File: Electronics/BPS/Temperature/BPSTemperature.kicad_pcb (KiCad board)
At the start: 2 copper layers, 0 parts

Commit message: Created PCB of Temperture Board for BPS
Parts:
- added C1: 1uF, Capacitor_SMD:C_0805_2012Metric, F.Cu at (66.6, 83.7)
- added C10: 1uF, Capacitor_SMD:C_0805_2012Metric, F.Cu at (66.7, 113.6)
- added C11: 1uF, Capacitor_SMD:C_0805_2012Metric, B.Cu at (66.6, 83.7)
- added C12: 1uF, Capacitor_SMD:C_0805_2012Metric, B.Cu at (66.6, 87.0)
- added C13: 1uF, Capacitor_SMD:C_0805_2012Metric, B.Cu at (66.6, 90.3)
- added C14: 1uF, Capacitor_SMD:C_0805_2012Metric, B.Cu at (66.6, 93.8)
- added C15: 1uF, Capacitor_SMD:C_0805_2012Metric, B.Cu at (66.6, 97.0)
- added C16: 1uF, Capacitor_SMD:C_0805_2012Metric, B.Cu at (66.6, 100.3)
- added C17: 1uF, Capacitor_SMD:C_0805_2012Metric, B.Cu at (66.6, 103.6)
- added C18: 1uF, Capacitor_SMD:C_0805_2012Metric, B.Cu at (66.6, 106.9)
- added C19: 1uF, Capacitor_SMD:C_0805_2012Metric, B.Cu at (66.7, 110.3)
- added C2: 1uF, Capacitor_SMD:C_0805_2012Metric, F.Cu at (66.5, 87.0)
- added C20: 1uF, Capacitor_SMD:C_0805_2012Metric, B.Cu at (66.6, 113.6)
- added C21: 0.1uF, Capacitor_SMD:C_0805_2012Metric, F.Cu at (90.5, 91.2)
- added C22: 10uF, Capacitor_SMD:C_0805_2012Metric, F.Cu at (93.3, 99.9)
- added C23: 10uF, Capacitor_SMD:C_0805_2012Metric, F.Cu at (88.5, 105.3)
- added C24: 10uF, Capacitor_SMD:C_0805_2012Metric, F.Cu at (92.3, 103.3)
- added C25: 1uF, Capacitor_SMD:C_0805_2012Metric, F.Cu at (87.5, 88.0)
- added C26: 1uF, Capacitor_SMD:C_0805_2012Metric, F.Cu at (83.4, 88.0)
- added C3: 1uF, Capacitor_SMD:C_0805_2012Metric, F.Cu at (66.6, 90.4)
- added C4: 1uF, Capacitor_SMD:C_0805_2012Metric, F.Cu at (66.6, 93.7)
- added C5: 1uF, Capacitor_SMD:C_0805_2012Metric, F.Cu at (66.5, 97.0)
- added C6: 1uF, Capacitor_SMD:C_0805_2012Metric, F.Cu at (66.6, 100.3)
- added C7: 1uF, Capacitor_SMD:C_0805_2012Metric, F.Cu at (66.6, 103.6)
- added C8: 1uF, Capacitor_SMD:C_0805_2012Metric, F.Cu at (66.5, 106.9)
- added C9: 1uF, Capacitor_SMD:C_0805_2012Metric, F.Cu at (66.6, 110.3)
- added D1: LED, LED_SMD:LED_0805_2012Metric, F.Cu at (103.1, 126.0)
- added J1: Conn_02x10_Counter_Clockwise, Connector_Molex:Molex_Micro-Fit_3.0_43045-2012_2x10_P3.00mm_Vertical, F.Cu at (54.1, 113.3)
- added J2: Logic Analyzer, Connector_PinHeader_2.54mm:PinHeader_1x05_P2.54mm_Vertical, F.Cu at (100.4, 129.7)
- added J3: Conn_02x06_Counter_Clockwise, UTSVT_Connectors:Molex_MicroFit3.0_2x6xP3.00mm_PolarizingPeg_Vertical, F.Cu at (121.1, 102.4)
- added J4: Conn_02x06_Counter_Clockwise, UTSVT_Connectors:Molex_MicroFit3.0_2x6xP3.00mm_PolarizingPeg_Vertical, F.Cu at (121.1, 79.7)
- added MH1: MountingHole, MountingHole:MountingHole_3mm, F.Cu at (53.0, 70.0)
- added MH2: MountingHole, MountingHole:MountingHole_3mm, F.Cu at (53.0, 129.0)
- added MH3: MountingHole, MountingHole:MountingHole_3mm, F.Cu at (122.0, 129.0)
- added MH4: MountingHole, MountingHole:MountingHole_3mm, F.Cu at (122.0, 70.0)
- added R1: 1k, Resistor_SMD:R_0805_2012Metric, F.Cu at (62.6, 83.7)
- added R10: 1k, Resistor_SMD:R_0805_2012Metric, F.Cu at (62.6, 113.6)
- added R11: 1k, Resistor_SMD:R_0805_2012Metric, B.Cu at (62.6, 83.7)
- added R12: 1k, Resistor_SMD:R_0805_2012Metric, B.Cu at (62.6, 87.0)
- added R13: 1k, Resistor_SMD:R_0805_2012Metric, B.Cu at (62.6, 90.3)
- added R14: 1k, Resistor_SMD:R_0805_2012Metric, B.Cu at (62.6, 93.8)
- added R15: 1k, Resistor_SMD:R_0805_2012Metric, B.Cu at (62.6, 97.0)
- added R16: 1k, Resistor_SMD:R_0805_2012Metric, B.Cu at (62.6, 100.3)
- added R17: 1k, Resistor_SMD:R_0805_2012Metric, B.Cu at (62.6, 103.6)
- added R18: 1k, Resistor_SMD:R_0805_2012Metric, B.Cu at (62.6, 106.9)
- added R19: 1k, Resistor_SMD:R_0805_2012Metric, B.Cu at (62.6, 110.3)
- added R2: 1k, Resistor_SMD:R_0805_2012Metric, F.Cu at (62.6, 87.0)
- added R20: 1k, Resistor_SMD:R_0805_2012Metric, B.Cu at (62.6, 113.6)
- added R3: 1k, Resistor_SMD:R_0805_2012Metric, F.Cu at (62.6, 90.4)
- added R4: 1k, Resistor_SMD:R_0805_2012Metric, F.Cu at (62.6, 93.7)
- added R5: 1k, Resistor_SMD:R_0805_2012Metric, F.Cu at (62.6, 97.0)
- added R6: 1k, Resistor_SMD:R_0805_2012Metric, F.Cu at (62.6, 100.3)
- added R7: 1k, Resistor_SMD:R_0805_2012Metric, F.Cu at (62.6, 103.6)
- added R8: 1k, Resistor_SMD:R_0805_2012Metric, F.Cu at (62.6, 106.9)
- added R9: 1k, Resistor_SMD:R_0805_2012Metric, F.Cu at (62.6, 110.3)
- added SW1: SW_DIP_x06, Button_Switch_SMD:SW_DIP_SPSTx06_Slide_Omron_A6S-610x_W8.9mm_P2.54mm, F.Cu at (105.3, 98.5)
- added TP1: TestPoint, TestPoint:TestPoint_Keystone_5005-5009_Compact, F.Cu at (83.4, 121.7)
- added TP2: TestPoint, TestPoint:TestPoint_Keystone_5005-5009_Compact, F.Cu at (63.5, 121.4)
- added U1: LTC2983, Package_QFP:LQFP-48_7x7mm_P0.5mm, F.Cu at (83.4, 98.0)
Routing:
- net GND: track 0.00 -> 88.3 mm, vias 0 -> 15
- net Net-(C11-Pad1): track 0.00 -> 33.8 mm, vias 0 -> 1
- net Net-(C12-Pad1): track 0.00 -> 33.4 mm, vias 0 -> 1
- net Net-(C13-Pad1): track 0.00 -> 32.5 mm, vias 0 -> 1
- net /CS2: track 0.00 -> 31.9 mm, vias 0 -> 1
- net Net-(C10-Pad1): track 0.00 -> 31.9 mm, vias 0 -> 2
- net /CS3: track 0.00 -> 31.8 mm, vias 0 -> 1
- net Net-(C14-Pad1): track 0.00 -> 31.4 mm, vias 0 -> 1
- net Net-(C15-Pad1): track 0.00 -> 30.8 mm, vias 0 -> 1
- net /CS4: track 0.00 -> 30.7 mm, vias 0 -> 1
- net /CS6: track 0.00 -> 30.5 mm, vias 0 -> 1
- net /CS5: track 0.00 -> 30.3 mm, vias 0 -> 1
- net Net-(C16-Pad1): track 0.00 -> 29.8 mm, vias 0 -> 1
- net /CS1: track 0.00 -> 29.7 mm, vias 0 -> 1
- net Net-(C17-Pad1): track 0.00 -> 27.2 mm, vias 0 -> 1
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- added copper zone on B.Cu, net GND
- added copper zone on F.Cu, net GND
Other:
- board outline added: 75 x 65 mm

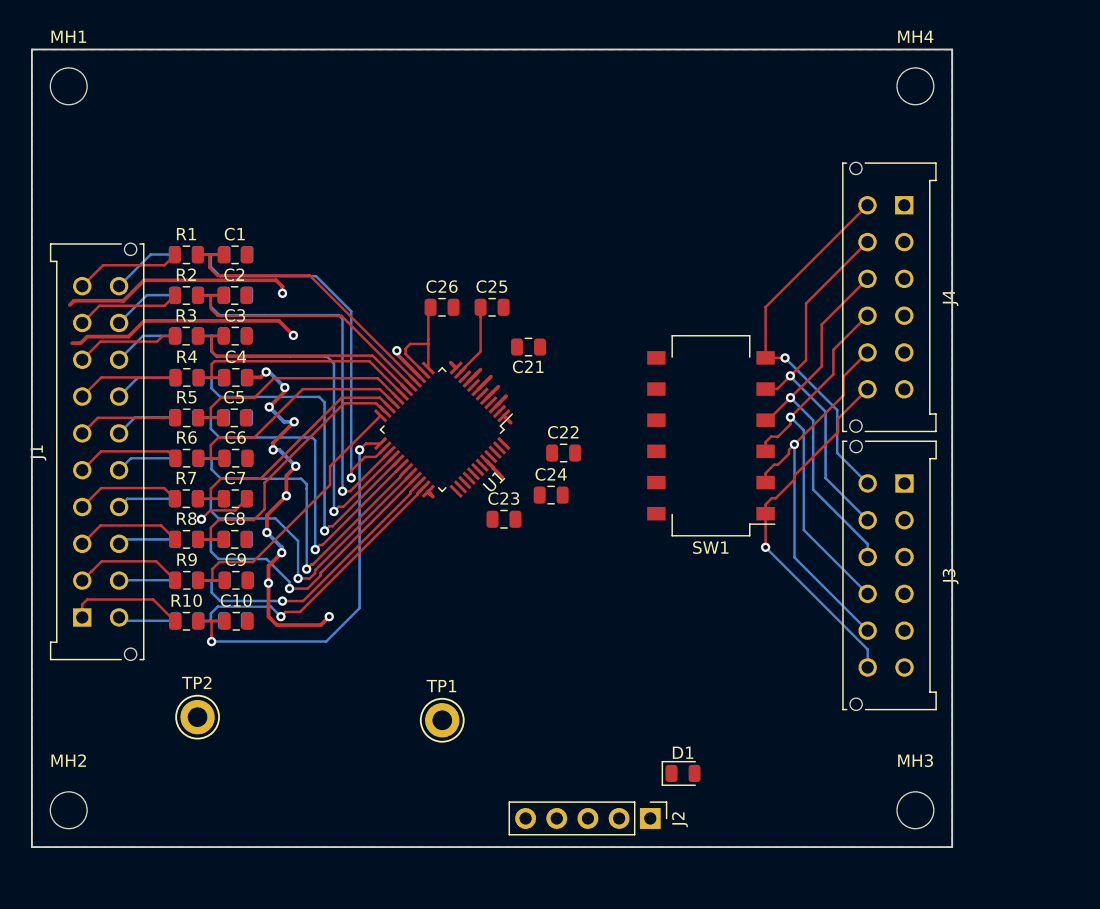
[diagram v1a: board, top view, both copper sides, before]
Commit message: Finished pcb layout of Temperature Board for BPS
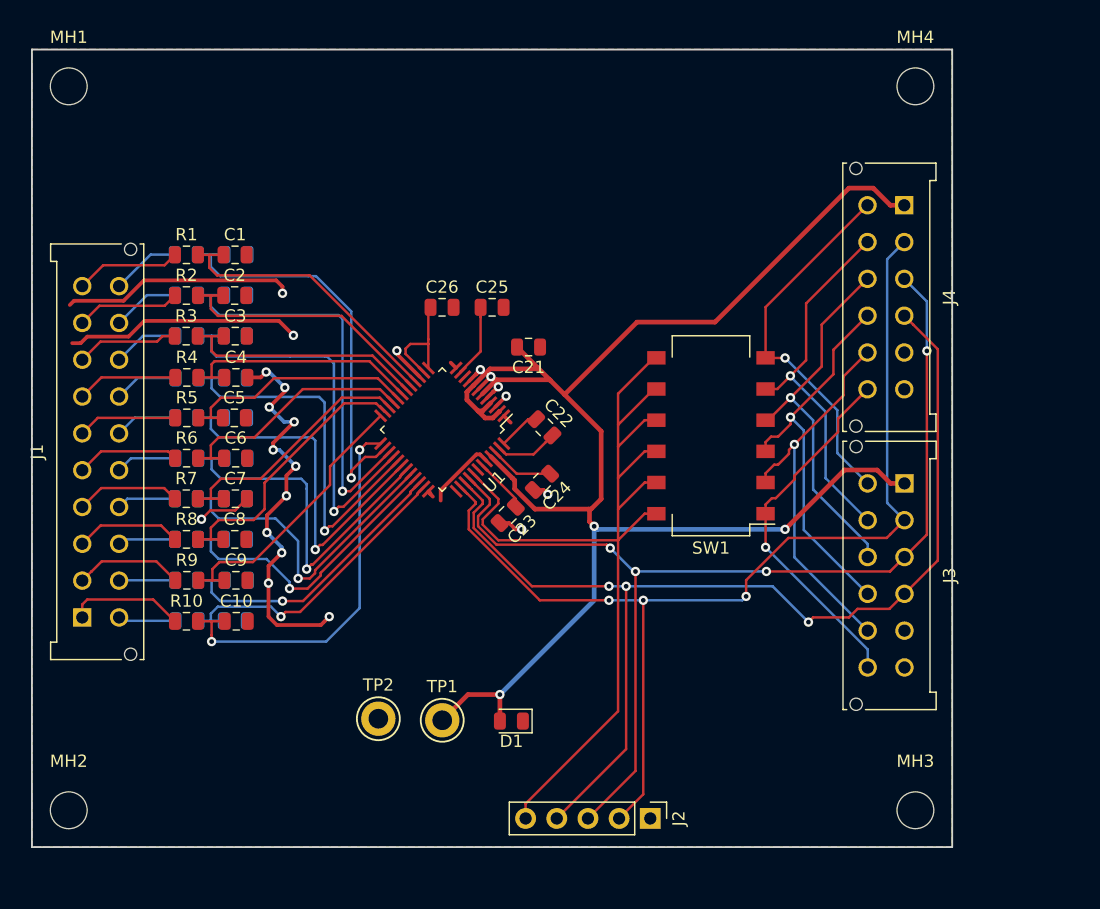
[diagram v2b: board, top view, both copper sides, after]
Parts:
- moved TP2 14.7 mm to (78.2, 121.5)
- moved D1 14.6 mm to (89.1, 121.7), turned to 180 degrees
- moved C22 2.62 mm to (91.8, 97.8), turned to 315 degrees
- moved C24 1.31 mm to (91.6, 102.2), turned to 225 degrees
- moved C23 0.46 mm to (88.8, 104.9), turned to 225 degrees
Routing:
- net +5V: track 0.00 -> 134.2 mm, vias 0 -> 3
- net /MISO: track 0.00 -> 90.0 mm, vias 0 -> 3
- net /SCK: track 0.00 -> 88.0 mm, vias 0 -> 3
- net /MOSI: track 0.00 -> 87.7 mm, vias 0 -> 4
- net /CS1_OUT: track 0.00 -> 79.5 mm
- net GND: track 88.3 -> 98.0 mm, vias 15 -> 21
- net Net-(C24-Pad1): track 0.00 -> 5.20 mm
- net Net-(C22-Pad2): track 0.00 -> 5.17 mm
- net Net-(C23-Pad1): track 0.00 -> 4.52 mm
- net Net-(C22-Pad1): track 0.00 -> 3.46 mm

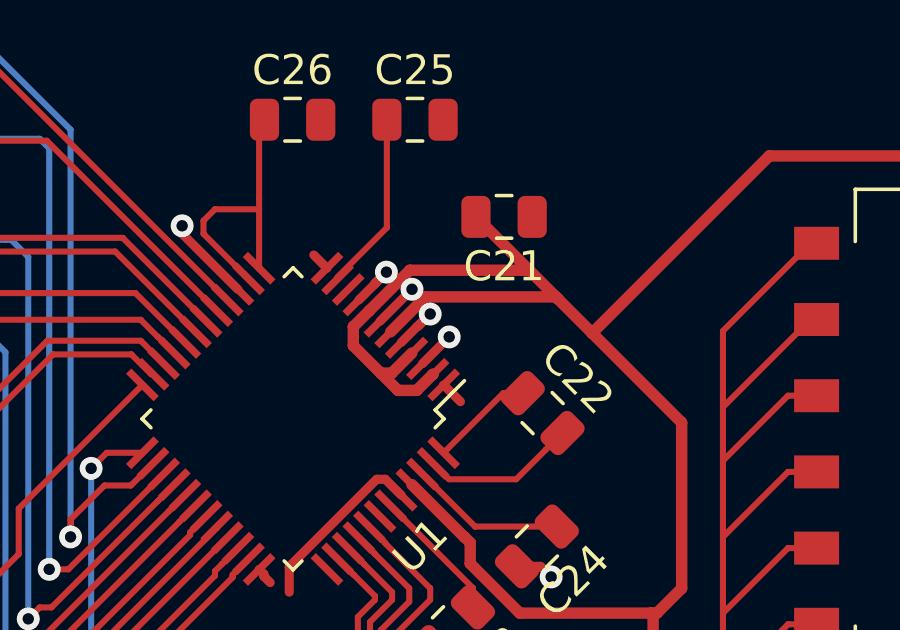
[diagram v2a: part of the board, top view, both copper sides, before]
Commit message: Edited pcb for Temperature Board, some issues remain
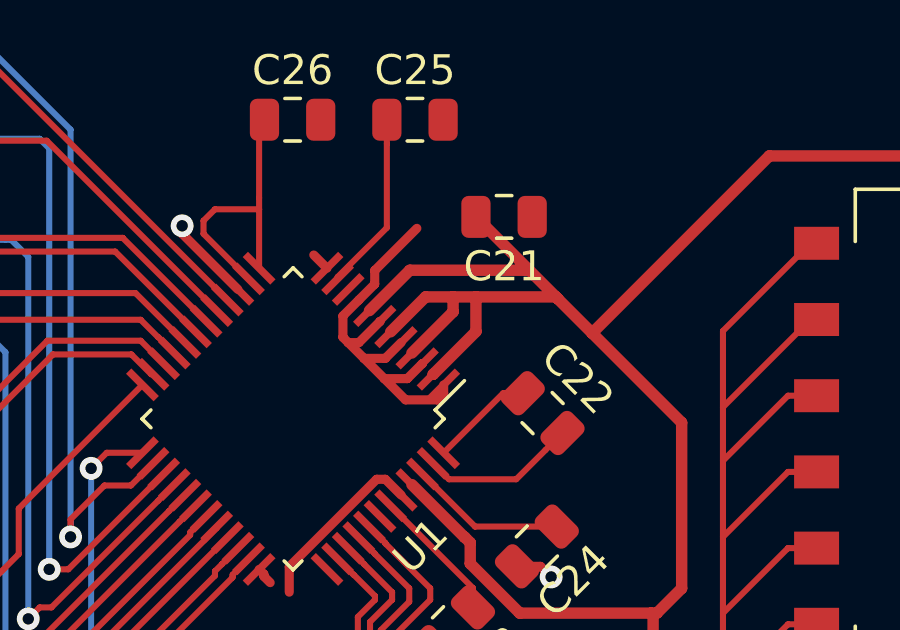
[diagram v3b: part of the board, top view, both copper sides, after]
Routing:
- net GND: track 98.0 -> 103.1 mm, vias 21 -> 17
- net +5V: track 134.2 -> 133.6 mm
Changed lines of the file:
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@@
   )
   (setup
-    (last_trace_width 0.381)
+    (last_trace_width 0.3048)
     (user_trace_width 0.2032)
     (user_trace_width 0.3048)
@@
   (segment (start 53.975 90.932) (end 53.2765 90.932) (width 0.3048) (layer F.Cu) (net 1))
   (segment (start 84.570371 92.960042) (end 84.129829 92.5195) (width 0.3048) (layer F.Cu) (net 1))
-  (segment (start 86.16136 93.490373) (end 86.5505 93.091) (width 0.3048) (layer F.Cu) (net 1))
-  (segment (start 85.631031 94.020702) (end 86.16136 93.490373) (width 0.3048) (layer F.Cu) (net 1))
-  (segment (start 86.16136 93.48014) (end 86.5505 93.091) (width 0.3048) (layer F.Cu) (net 1))
-  (segment (start 86.338138 94.727809) (end 87.403447 93.6625) (width 0.3048) (layer F.Cu) (net 1))
-  (segment (start 87.575574 94.904587) (end 88.011 94.488) (width 0.3048) (layer F.Cu) (net 1))
-  (segment (start 87.045245 95.434916) (end 87.575574 94.904587) (width 0.3048) (layer F.Cu) (net 1))
-  (segment (start 87.594413 94.904587) (end 88.011 94.488) (width 0.3048) (layer F.Cu) (net 1))
-  (segment (start 87.752351 96.142022) (end 88.644373 95.25) (width 0.3048) (layer F.Cu) (net 1))
-  (segment (start 88.459458 96.849129) (end 89.019329 97.409) (width 0.3048) (layer F.Cu) (net 1))
   (segment (start 82.466727 103.160056) (end 82.466727 103.231227) (width 0.3048) (layer F.Cu) (net 1))
   (segment (start 82.307629 103.000958) (end 82.466727 103.160056) (width 0.3048) (layer F.Cu) (net 1))
@@
   (segment (start 88.895553 105.592826) (end 89.284227 105.9815) (width 0.3048) (layer F.Cu) (net 1))
   (segment (start 88.110087 105.592826) (end 88.895553 105.592826) (width 0.3048) (layer F.Cu) (net 1))
-  (segment (start 87.403447 93.6625) (end 87.403447 93.6625) (width 0.3048) (layer F.Cu) (net 1))
-  (via (at 87.403447 93.6625) (size 0.762) (drill 0.381) (layers F.Cu B.Cu) (net 1))
-  (segment (start 88.011 94.488) (end 87.594413 94.904587) (width 0.3048) (layer F.Cu) (net 1))
-  (via (at 88.011 94.488) (size 0.762) (drill 0.381) (layers F.Cu B.Cu) (net 1))
-  (segment (start 86.5505 93.091) (end 86.16136 93.48014) (width 0.3048) (layer F.Cu) (net 1))
-  (via (at 86.5505 93.091) (size 0.762) (drill 0.381) (layers F.Cu B.Cu) (net 1))
-  (segment (start 88.644373 95.25) (end 88.644373 95.25) (width 0.3048) (layer F.Cu) (net 1))
-  (via (at 88.644373 95.25) (size 0.762) (drill 0.381) (layers F.Cu B.Cu) (net 1))
   (segment (start 91.689553 102.897913) (end 92.04264 103.251) (width 0.3048) (layer F.Cu) (net 1))
   (segment (start 90.904087 102.897913) (end 91.689553 102.897913) (width 0.3048) (layer F.Cu) (net 1))
@@
   (segment (start 89.284227 106.015542) (end 89.377185 106.1085) (width 0.3048) (layer F.Cu) (net 1))
   (segment (start 89.284227 105.9815) (end 89.284227 106.015542) (width 0.3048) (layer F.Cu) (net 1))
+  (segment (start 86.16136 93.490373) (end 86.16136 93.03564) (width 0.3048) (layer F.Cu) (net 1))
+  (segment (start 85.631031 94.020702) (end 86.16136 93.490373) (width 0.3048) (layer F.Cu) (net 1))
+  (segment (start 86.16136 93.03564) (end 87.5665 91.6305) (width 0.3048) (layer F.Cu) (net 1))
+  (segment (start 86.338138 94.734441) (end 85.632079 95.4405) (width 0.3048) (layer F.Cu) (net 1))
+  (segment (start 86.338138 94.727809) (end 86.338138 94.734441) (width 0.3048) (layer F.Cu) (net 1))
+  (segment (start 85.632079 95.4405) (end 85.2805 95.4405) (width 0.3048) (layer F.Cu) (net 1))
+  (segment (start 85.100702 94.551031) (end 85.631031 94.020702) (width 0.3048) (layer F.Cu) (net 1))
+  (segment (start 85.100702 95.260702) (end 85.100702 94.551031) (width 0.3048) (layer F.Cu) (net 1))
+  (segment (start 85.2805 95.4405) (end 85.100702 95.260702) (width 0.3048) (layer F.Cu) (net 1))
+  (segment (start 85.805245 95.965245) (end 85.2805 95.4405) (width 0.3048) (layer F.Cu) (net 1))
+  (segment (start 86.514916 95.965245) (end 85.805245 95.965245) (width 0.3048) (layer F.Cu) (net 1))
+  (segment (start 87.045245 95.434916) (end 86.514916 95.965245) (width 0.3048) (layer F.Cu) (net 1))
+  (segment (start 86.481287 96.641287) (end 85.805245 95.965245) (width 0.3048) (layer F.Cu) (net 1))
+  (segment (start 87.246454 96.641287) (end 86.481287 96.641287) (width 0.3048) (layer F.Cu) (net 1))
+  (segment (start 87.745719 96.142022) (end 87.246454 96.641287) (width 0.3048) (layer F.Cu) (net 1))
+  (segment (start 87.752351 96.142022) (end 87.745719 96.142022) (width 0.3048) (layer F.Cu) (net 1))
+  (segment (start 87.188394 97.348394) (end 86.481287 96.641287) (width 0.3048) (layer F.Cu) (net 1))
+  (segment (start 88.23697 97.348394) (end 87.188394 97.348394) (width 0.3048) (layer F.Cu) (net 1))
+  (segment (start 88.459458 97.125906) (end 88.23697 97.348394) (width 0.3048) (layer F.Cu) (net 1))
+  (segment (start 88.459458 96.849129) (end 88.459458 97.125906) (width 0.3048) (layer F.Cu) (net 1))
   (segment (start 64.5795 83.734656) (end 65.615913 83.734656) (width 0.2032) (layer F.Cu) (net 2))
   (segment (start 64.4525 83.734656) (end 64.5795 83.734656) (width 0.2032) (layer F.Cu) (net 2))
@@
   (segment (start 91.2495 92.964) (end 89.535 91.2495) (width 0.381) (layer F.Cu) (net 22))
   (segment (start 92.202 93.9165) (end 92.2655 93.98) (width 0.381) (layer F.Cu) (net 22))
-  (segment (start 87.856553 93.9165) (end 92.202 93.9165) (width 0.381) (layer F.Cu) (net 22))
   (segment (start 86.691691 95.081362) (end 87.856553 93.9165) (width 0.381) (layer F.Cu) (net 22))
   (segment (start 92.2655 93.98) (end 91.2495 92.964) (width 0.381) (layer F.Cu) (net 22))
-  (segment (start 86.730767 96.4565) (end 86.36 96.4565) (width 0.381) (layer F.Cu) (net 22))
-  (segment (start 87.398798 95.788469) (end 86.730767 96.4565) (width 0.381) (layer F.Cu) (net 22))
-  (segment (start 85.454255 94.904584) (end 85.984584 94.374255) (width 0.381) (layer F.Cu) (net 22))
-  (segment (start 85.44722 94.911619) (end 85.454255 94.904584) (width 0.381) (layer F.Cu) (net 22))
-  (segment (start 85.44722 95.54372) (end 85.44722 94.911619) (width 0.381) (layer F.Cu) (net 22))
-  (segment (start 86.36 96.4565) (end 85.44722 95.54372) (width 0.381) (layer F.Cu) (net 22))
-  (segment (start 86.93644 97.03294) (end 86.36 96.4565) (width 0.381) (layer F.Cu) (net 22))
-  (segment (start 87.561907 97.03294) (end 86.93644 97.03294) (width 0.381) (layer F.Cu) (net 22))
-  (segment (start 88.099271 96.495576) (end 87.561907 97.03294) (width 0.381) (layer F.Cu) (net 22))
-  (segment (start 88.105905 96.495576) (end 88.099271 96.495576) (width 0.381) (layer F.Cu) (net 22))
   (segment (start 89.154 101.927733) (end 87.398798 100.172531) (width 0.381) (layer F.Cu) (net 22))
   (segment (start 89.164233 101.927733) (end 89.154 101.927733) (width 0.381) (layer F.Cu) (net 22))
@@
   (segment (start 85.5345 119.5705) (end 83.439 121.666) (width 0.381) (layer F.Cu) (net 22))
   (segment (start 88.138 119.5705) (end 85.5345 119.5705) (width 0.381) (layer F.Cu) (net 22))
+  (segment (start 88.773 94.414267) (end 88.773 93.9165) (width 0.381) (layer F.Cu) (net 22))
+  (segment (start 87.398798 95.788469) (end 88.773 94.414267) (width 0.381) (layer F.Cu) (net 22))
+  (segment (start 87.856553 93.9165) (end 88.773 93.9165) (width 0.381) (layer F.Cu) (net 22))
+  (segment (start 89.535 95.073113) (end 89.535 93.9165) (width 0.381) (layer F.Cu) (net 22))
+  (segment (start 88.112537 96.495576) (end 89.535 95.073113) (width 0.381) (layer F.Cu) (net 22))
+  (segment (start 88.105905 96.495576) (end 88.112537 96.495576) (width 0.381) (layer F.Cu) (net 22))
+  (segment (start 88.773 93.9165) (end 89.535 93.9165) (width 0.381) (layer F.Cu) (net 22))
+  (segment (start 89.535 93.9165) (end 92.202 93.9165) (width 0.381) (layer F.Cu) (net 22))
   (segment (start 90.444242 97.127087) (end 91.094587 97.127087) (width 0.2032) (layer F.Cu) (net 23))
   (segment (start 88.459458 99.111871) (end 90.444242 97.127087) (width 0.2032) (layer F.Cu) (net 23))
